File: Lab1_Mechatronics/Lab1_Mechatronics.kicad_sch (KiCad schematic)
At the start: 13 parts, among them Q1 NMOS

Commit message: fixed wording, dumet electrode -> neon bulb
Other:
- note added: "Neon Bulb"
- note removed: "Dumet Electrode"
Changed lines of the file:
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@@
     (effects (font (size 1.1 1.1) (color 0 0 0 1)) (justify left bottom))
   )
-  (text "Dumet\nElectrode" (at 48.26 77.47 0)
+  (text "Neon \nBulb" (at 50.8 77.47 0)
     (effects (font (size 1.1 1.1) (color 0 0 0 1)) (justify left bottom))
   )
-  (text "Dumet\nElectrode" (at 48.26 123.19 0)
+  (text "Neon \nBulb" (at 50.8 123.19 0)
     (effects (font (size 1.1 1.1) (color 0 0 0 1)) (justify left bottom))
   )
-  (text "Dumet\nElectrode" (at 48.26 36.83 0)
+  (text "Neon\nBulb" (at 50.8 36.83 0)
     (effects (font (size 1.1 1.1) (color 0 0 0 1)) (justify left bottom))
   )

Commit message: added NE2 to neon bulb
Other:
- note added: "NE2 Neon Bulb"
- note removed: "Neon Bulb"
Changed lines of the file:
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@@
     (effects (font (size 1.1 1.1) (color 0 0 0 1)) (justify left bottom))
   )
-  (text "Neon \nBulb" (at 50.8 77.47 0)
+  (text "NE2\nNeon \nBulb" (at 50.8 77.47 0)
     (effects (font (size 1.1 1.1) (color 0 0 0 1)) (justify left bottom))
   )
-  (text "Neon \nBulb" (at 50.8 123.19 0)
+  (text "NE2\nNeon \nBulb" (at 50.8 123.19 0)
     (effects (font (size 1.1 1.1) (color 0 0 0 1)) (justify left bottom))
   )
-  (text "Neon\nBulb" (at 50.8 36.83 0)
+  (text "NE2\nNeon\nBulb" (at 50.8 36.83 0)
     (effects (font (size 1.1 1.1) (color 0 0 0 1)) (justify left bottom))
   )

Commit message: added pngs, temporary?
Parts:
- added MES4, MES5: Oscilloscope, symbol Device:Oscilloscope
- added R2, R3: 1k, symbol Device:R_US
- added V4: 12, symbol Simulation_SPICE:VDC
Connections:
- net GND: now also MES4.1 (-), MES5.1 (-), R2.2, R3.2, V4.2
- new net BLUE_BANANA_JACK: MES5.2 (+), R3.1
- new net GREEN_BANANA_JACK(LOWER_SWITCH): MES4.2 (+), R2.1
- new net WHITE_BANANA_JACK: V4.1

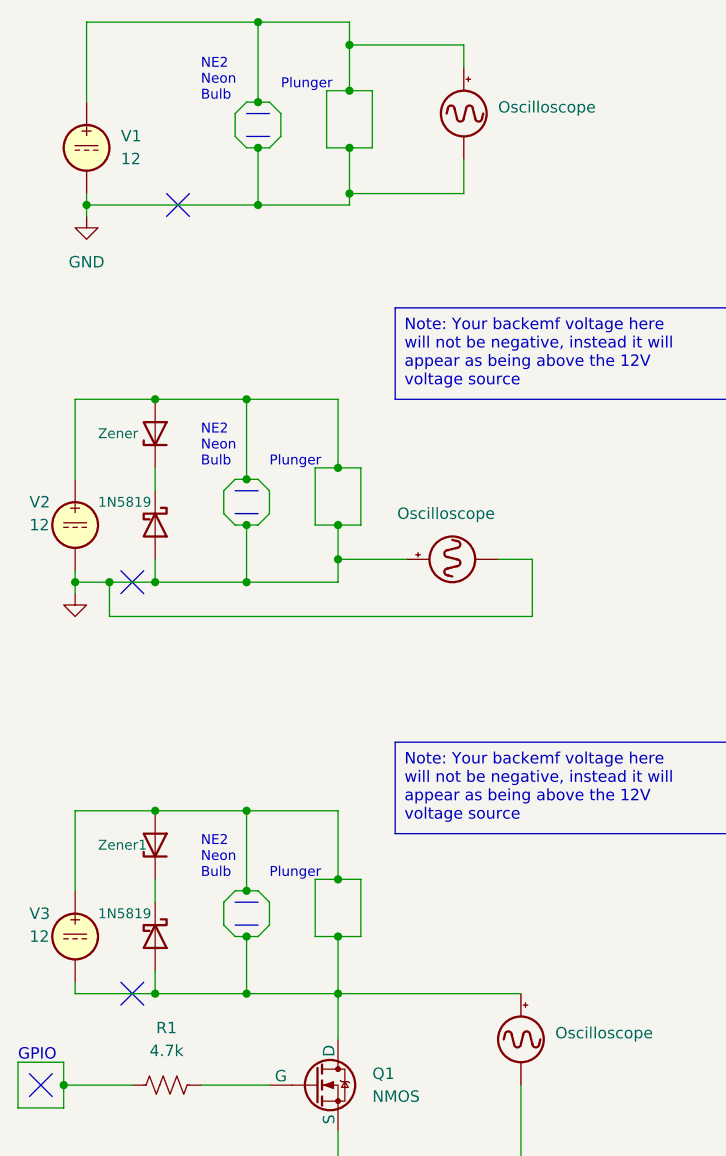
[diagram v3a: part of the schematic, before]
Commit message: using pdf instead of png
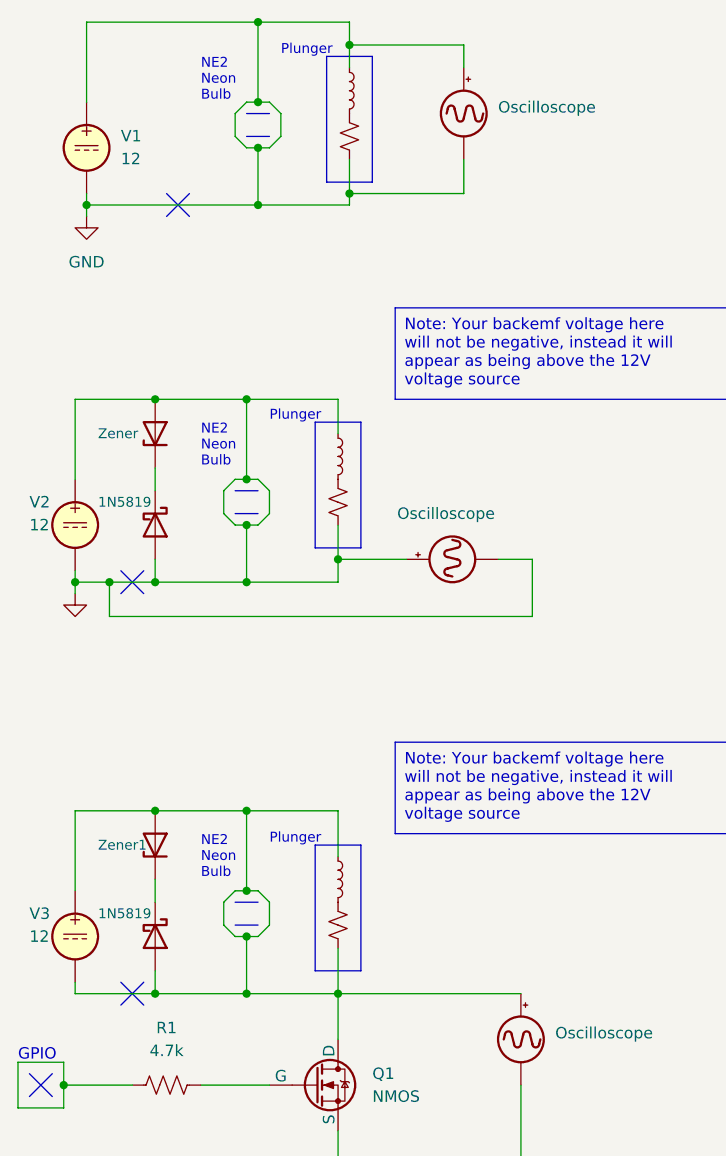
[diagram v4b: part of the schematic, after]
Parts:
- added L1, L2, L3: L_Small, symbol Device:L_Small
- added R4, R5, R6: R_Small_US, symbol Device:R_Small_US
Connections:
- net GND: now also L1.1, L2.1, R4.2, R5.2
- net at D2.2 (A), MES3.2 (+), Q1.1 (D)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: now also L3.1, R6.2
- new net: L1.2, R4.1
- new net: L2.2, R5.1
- new net: L3.2, R6.1

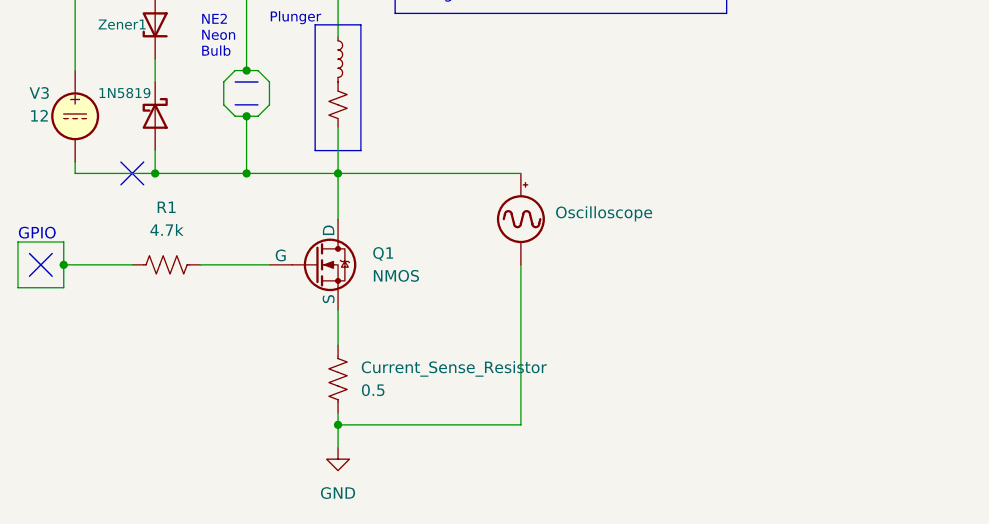
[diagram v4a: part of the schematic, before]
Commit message: fixed 3rd schematic that connected source ground to 'negative' side of coil
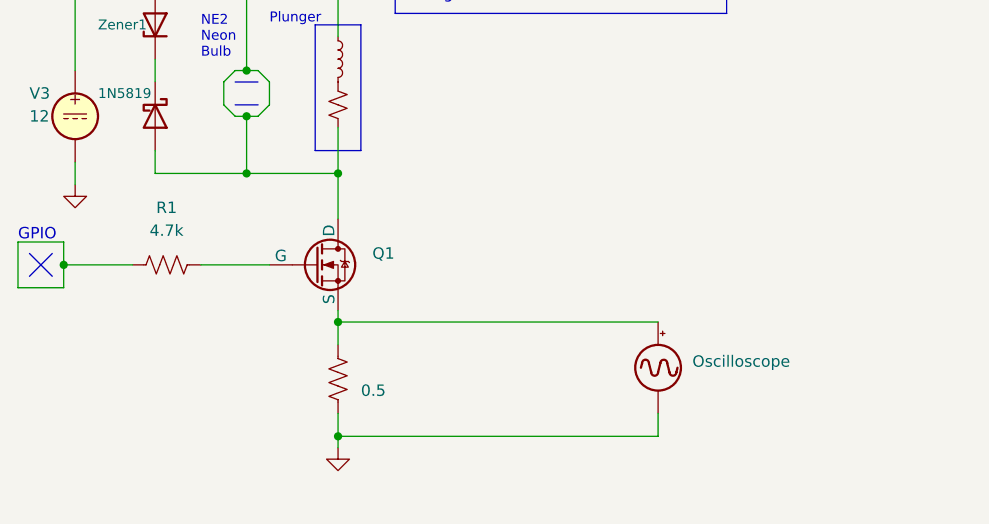
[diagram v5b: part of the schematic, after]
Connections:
- net GND: now also V3.2
- net at D2.2 (A), L3.1, Q1.1 (D)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: no longer MES3.2 (+), V3.2
- net at Current_Sense_Resistor.1, Q1.3 (S): now also MES3.2 (+)
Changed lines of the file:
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@@
   (junction (at 57.15 27.94) (diameter 0) (color 0 0 0 0)
   )
-  (junction (at 45.72 135.89) (diameter 0) (color 0 0 0 0)
-  )
   (junction (at 55.88 78.74) (diameter 0) (color 0 0 0 0)
   )
@@
   (junction (at 55.88 124.46) (diameter 0) (color 0 0 0 0)
   )
-  (junction (at 66.04 163.83) (diameter 0) (color 0 0 0 0)
-  )
   (junction (at 35.56 146.05) (diameter 0) (color 0 0 0 0)
   )
@@
   (junction (at 149.86 96.52) (diameter 0) (color 0 0 0 0)
   )
+  (junction (at 66.04 152.4) (diameter 0) (color 0 0 0 0)
+  )
   (junction (at 40.64 90.17) (diameter 0) (color 0 0 0 0)
   )
@@
   (junction (at 55.88 69.85) (diameter 0) (color 0 0 0 0)
   )
+  (junction (at 66.04 165.1) (diameter 0) (color 0 0 0 0)
+  )
   (junction (at 38.1 48.26) (diameter 0) (color 0 0 0 0)
   )
@@
   )
   (wire (pts (xy 57.15 27.94) (xy 57.15 36.83))
-    (stroke (width 0) (type default))
-  )
-  (wire (pts (xy 66.04 163.83) (xy 66.04 166.37))
     (stroke (width 0) (type default))
   )
@@
     (stroke (width 0) (type default))
   )
-  (wire (pts (xy 66.04 162.56) (xy 66.04 163.83))
+  (wire (pts (xy 66.04 162.56) (xy 66.04 165.1))
     (stroke (width 0) (type default))
   )
@@
     (stroke (width 0) (type default) (color 125 0 0 1))
   )
+  (wire (pts (xy 101.6 162.56) (xy 101.6 165.1))
+    (stroke (width 0) (type default) (color 0 0 255 1))
+  )
   (wire (pts (xy 67.31 46.99) (xy 67.31 48.26))
     (stroke (width 0) (type default))
   )
-  (wire (pts (xy 66.04 135.89) (xy 86.36 135.89))
-    (stroke (width 0) (type default) (color 255 0 0 1))
-  )
   (wire (pts (xy 55.88 83.82) (xy 55.88 90.17))
     (stroke (width 0) (type default))
@@
   )
   (polyline (pts (xy 63.5 133.35) (xy 68.58 133.35))
-    (stroke (width 0) (type default))
-  )
-  (wire (pts (xy 36.83 134.62) (xy 36.83 135.89))
     (stroke (width 0) (type default))
   )
@@
     (stroke (width 0) (type default) (color 255 169 0 1))
   )
-  (polyline (pts (xy 41.91 134.62) (xy 44.45 137.16))
-    (stroke (width 0) (type default) (color 125 0 0 1))
-  )
   (wire (pts (xy 55.88 115.57) (xy 55.88 124.46))
     (stroke (width 0) (type default))
@@
     (stroke (width 0) (type default))
   )
-  (wire (pts (xy 36.83 135.89) (xy 45.72 135.89))
-    (stroke (width 0) (type default))
-  )
   (wire (pts (xy 40.64 90.17) (xy 45.72 90.17))
     (stroke (width 0) (type default))
@@
     (stroke (width 0) (type default) (color 0 0 1 1))
   )
-  (wire (pts (xy 66.04 151.13) (xy 66.04 154.94))
+  (wire (pts (xy 66.04 151.13) (xy 66.04 152.4))
     (stroke (width 0) (type default))
   )
@@
     (stroke (width 0) (type default))
   )
+  (wire (pts (xy 66.04 152.4) (xy 66.04 154.94))
+    (stroke (width 0) (type default))
+  )
   (wire (pts (xy 45.72 135.89) (xy 55.88 135.89))
     (stroke (width 0) (type default))
@@
     (stroke (width 0) (type default))
   )
+  (wire (pts (xy 66.04 165.1) (xy 101.6 165.1))
+    (stroke (width 0) (type default) (color 0 0 255 1))
+  )
   (wire (pts (xy 36.83 115.57) (xy 36.83 124.46))
     (stroke (width 0) (type default))
@@
   (polyline (pts (xy 31.75 147.32) (xy 34.29 144.78))
     (stroke (width 0) (type default) (color 0 0 1 1))
+  )
+  (wire (pts (xy 66.04 152.4) (xy 101.6 152.4))
+    (stroke (width 0) (type default) (color 255 0 0 1))
   )
   (wire (pts (xy 55.88 124.46) (xy 57.15 124.46))
@@
     (stroke (width 0) (type default) (color 0 0 255 1))
   )
+  (wire (pts (xy 66.04 165.1) (xy 66.04 166.37))
+    (stroke (width 0) (type default))
+  )
   (polyline (pts (xy 66.04 72.39) (xy 68.58 72.39))
     (stroke (width 0) (type default))
@@
     (stroke (width 0) (type default))
   )
+  (wire (pts (xy 36.83 134.62) (xy 36.83 137.16))
+    (stroke (width 0) (type default))
+  )
   (wire (pts (xy 30.48 143.51) (xy 35.56 143.51))
     (stroke (width 0) (type default))
-  )
-  (wire (pts (xy 66.04 163.83) (xy 86.36 163.83))
-    (stroke (width 0) (type default) (color 0 0 255 1))
   )
   (wire (pts (xy 55.88 83.82) (xy 57.15 83.82))
@@
     (stroke (width 0) (type default) (color 0 0 1 1))
   )
-  (wire (pts (xy 86.36 146.05) (xy 86.36 163.83))
-    (stroke (width 0) (type default) (color 0 0 255 1))
-  )
   (wire (pts (xy 54.61 129.54) (xy 55.88 129.54))
     (stroke (width 0) (type default) (color 10 0 0 1))
@@
     (stroke (width 0) (type default))
   )
-  (polyline (pts (xy 44.45 134.62) (xy 41.91 137.16))
-    (stroke (width 0) (type default) (color 125 0 0 1))
-  )
   (wire (pts (xy 40.64 93.98) (xy 87.63 93.98))
     (stroke (width 0) (type default) (color 0 0 255 1))
@@
         (path "/69db5f8a-c07c-40c0-8780-af495b77f2db"
           (reference "#PWR05") (unit 1)
+        )
+      )
+    )
+  )
+  (symbol (lib_id "power:GND") (at 36.83 137.16 0) (unit 1)
+    (in_bom yes) (on_board yes) (dnp no)
+    (property "Reference" "#PWR07" (at 36.83 143.51 0)
+      (effects (font (size 1.27 1.27)) hide)
+    )
+    (property "Value" "GND" (at 31.75 138.43 0)
+      (effects (font (size 1.27 1.27) (color 0 0 1 1)) hide)
+    )
+    (property "Footprint" "" (at 36.83 137.16 0)
+      (effects (font (size 1.27 1.27)) hide)
+    )
+    (property "Datasheet" "" (at 36.83 137.16 0)
+      (effects (font (size 1.27 1.27)) hide)
+    )
+    (pin "1")
+    (instances
+      (project "Lab1_Mechatronics"
+        (path "/69db5f8a-c07c-40c0-8780-af495b77f2db"
+          (reference "#PWR07") (unit 1)
         )
       )
@@
     (in_bom yes) (on_board yes) (dnp no) (fields_autoplaced)
     (property "Reference" "Current_Sense_Resistor" (at 68.58 157.48 0)
-      (effects (font (size 1.27 1.27) (color 0 0 1 1)) (justify left))
+      (effects (font (size 1.27 1.27) (color 0 0 1 1)) (justify left) hide)
     )
     (property "Value" "0.5" (at 68.58 160.02 0)
@@
     )
     (property "Value" "Oscilloscope" (at 83.82 37.4015 0)
-      (effects (font (size 1.27 1.27)) (justify left))
+      (effects (font (size 1.27 1.27) (color 0 0 1 1)) (justify left))
     )
     (property "Footprint" "" (at 80.01 35.56 90)
@@
         (path "/69db5f8a-c07c-40c0-8780-af495b77f2db"
           (reference "#PWR01") (unit 1)
-        )
-      )
-    )
-  )
-  (symbol (lib_id "Device:Oscilloscope") (at 86.36 140.97 0) (unit 1)
-    (in_bom yes) (on_board yes) (dnp no)
-    (property "Reference" "MES3" (at 90.17 139.0015 0)
-      (effects (font (size 1.27 1.27)) (justify left) hide)
-    )
-    (property "Value" "Oscilloscope" (at 90.17 140.2715 0)
-      (effects (font (size 1.27 1.27) (color 0 0 1 1)) (justify left))
-    )
-    (property "Footprint" "" (at 86.36 138.43 90)
-      (effects (font (size 1.27 1.27)) hide)
-    )
-    (property "Datasheet" "~" (at 86.36 138.43 90)
-      (effects (font (size 1.27 1.27)) hide)
-    )
-    (pin "1")
-    (pin "2")
-    (instances
-      (project "Lab1_Mechatronics"
-        (path "/69db5f8a-c07c-40c0-8780-af495b77f2db"
-          (reference "MES3") (unit 1)
         )
       )
@@
     )
     (property "Value" "NMOS" (at 69.85 147.32 0)
-      (effects (font (size 1.27 1.27) (color 0 0 1 1)) (justify left))
+      (effects (font (size 1.27 1.27) (color 0 0 1 1)) (justify left) hide)
     )
     (property "Footprint" "" (at 68.58 143.51 0)
@@
     (in_bom yes) (on_board yes) (dnp no) (fields_autoplaced)
     (property "Reference" "V1" (at 41.91 40.6042 0)
-      (effects (font (size 1.27 1.27)) (justify left))
+      (effects (font (size 1.27 1.27) (color 0 0 1 1)) (justify left))
     )
     (property "Value" "12" (at 41.91 43.1442 0)
-      (effects (font (size 1.27 1.27)) (justify left))
+      (effects (font (size 1.27 1.27) (color 0 0 1 1)) (justify left))
     )
     (property "Footprint" "" (at 38.1 41.91 0)
@@
     )
     (property "Value" "GND" (at 66.04 171.45 0)
-      (effects (font (size 1.27 1.27)))
+      (effects (font (size 1.27 1.27)) hide)
     )
     (property "Footprint" "" (at 66.04 166.37 0)
@@
         )
       )
+    )
+  )
+  (symbol (lib_id "Device:Oscilloscope") (at 101.6 157.48 0) (unit 1)
+    (in_bom yes) (on_board yes) (dnp no)
+    (property "Reference" "MES3" (at 105.41 155.5115 0)
+      (effects (font (size 1.27 1.27)) (justify left) hide)
+    )
+    (property "Value" "Oscilloscope" (at 105.41 156.7815 0)
+      (effects (font (size 1.27 1.27) (color 0 0 1 1)) (justify left))
+    )
+    (property "Footprint" "" (at 101.6 154.94 90)
+      (effects (font (size 1.27 1.27)) hide)
+    )
+    (property "Datasheet" "~" (at 101.6 154.94 90)
+      (effects (font (size 1.27 1.27)) hide)
+    )
+    (pin "1")
+    (pin "2")
+    (instances
+      (project "Lab1_Mechatronics"
+        (path "/69db5f8a-c07c-40c0-8780-af495b77f2db"
+          (reference "MES3") (unit 1)
+        )
+      )
